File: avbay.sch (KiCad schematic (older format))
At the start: 19 parts, among them P1 CONN_2, P2 CONN_6, P3 CONN_2, P4 CONN_2, P6 CONN_01X12, SW2 SW_PUSH, SW3 SW_PUSH, U2 XBEE

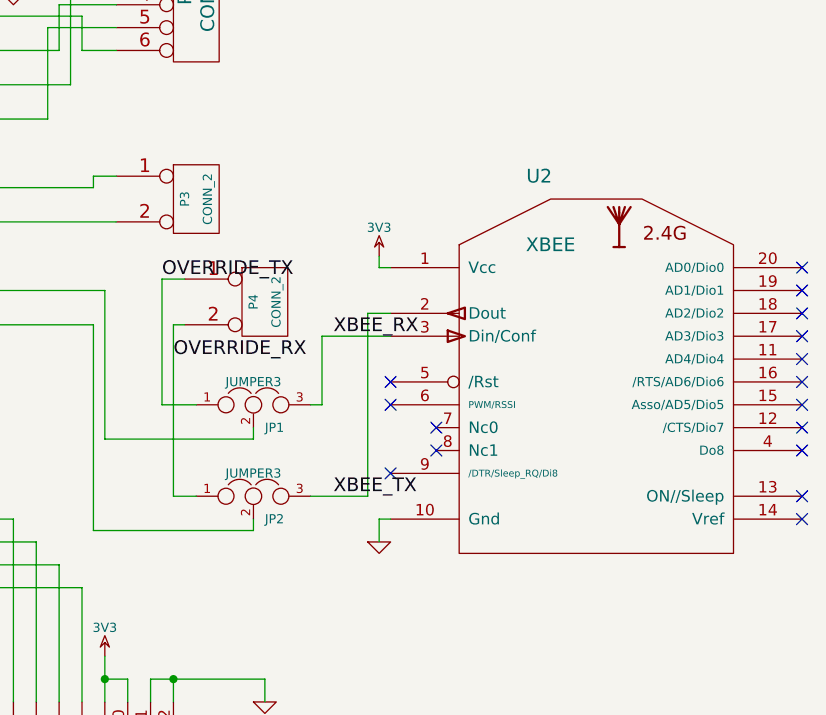
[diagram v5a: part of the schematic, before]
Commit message: Changed stuff
Layed out board with regulators, leds, and GPIOs
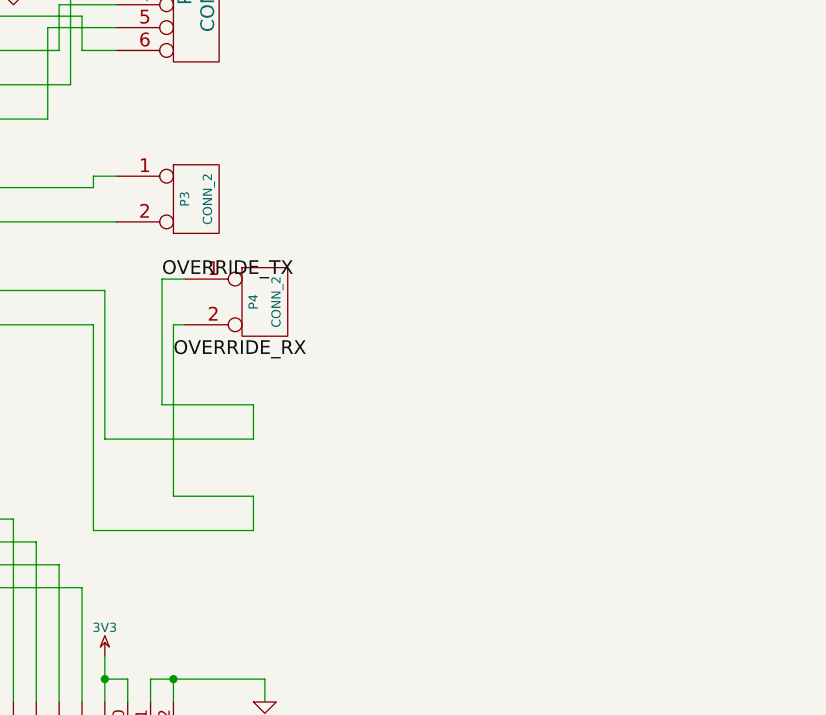
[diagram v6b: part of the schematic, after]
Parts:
- removed JP1, JP2: JUMPER3, ~, symbol JUMPER3
- removed U2: XBEE, symbol XBEE
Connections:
- no-connect marks 16 -> 0

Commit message: Made breakout board
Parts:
- removed BT1: BATTERY, ~, symbol BATTERY
- removed D1, D2, D3, D4: LED, symbol LED
- removed P1, P3, P4: CONN_2, symbol CONN_2
- removed P2: CONN_6, symbol CONN_6
- removed P6: CONN_01X12, symbol CONN_01X12
- removed R2, R3, R4, R5: 48, symbol R
- removed SW2, SW3: SW_PUSH, symbol SW_PUSH
- added P1, P2: CONN_01X06, Pin_Headers:Pin_Header_Straight_1x06, symbol CONN_01X06
- added P3: CONN_01X04, Pin_Headers:Pin_Header_Straight_1x04, symbol CONN_01X04
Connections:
- net 3V3: now also P1.4 (P4), P1.5 (P5), P1.6 (P6), P2.1 (P1)
- net GND: now also P1.1 (P1), P1.2 (P2), P1.3 (P3), P2.3 (P3)
- net MCU/JTCK-SWCLK: now also P2.2 (P2)
- net MCU/JTDO-SWO: now also P2.6 (P6)
- net MCU/JTMS-SWDIO: now also P2.4 (P4)
- net MCU/NRST: now also P2.5 (P5)
- net MCU/USART_RX: now also P3.4 (P4)
- net MCU/USART_TX: now also P3.3 (P3)
- new net MCU/RADIO_RX: P3.2 (P2)
- new net MCU/RADIO_TX: P3.1 (P1)
